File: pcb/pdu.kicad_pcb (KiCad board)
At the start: 2 copper layers, 210 x 105.5 mm, 22 parts, among them J1 XT90-F, J10 XT60-F, J12 Conn_02x06_Odd_Even, J2 XT90-M, J3 XT90-M, J4 XT90-F, J5 XT60-F, J6 XT60-F, J7 XT60-F, J8 XT60-F, J9 XT60-F

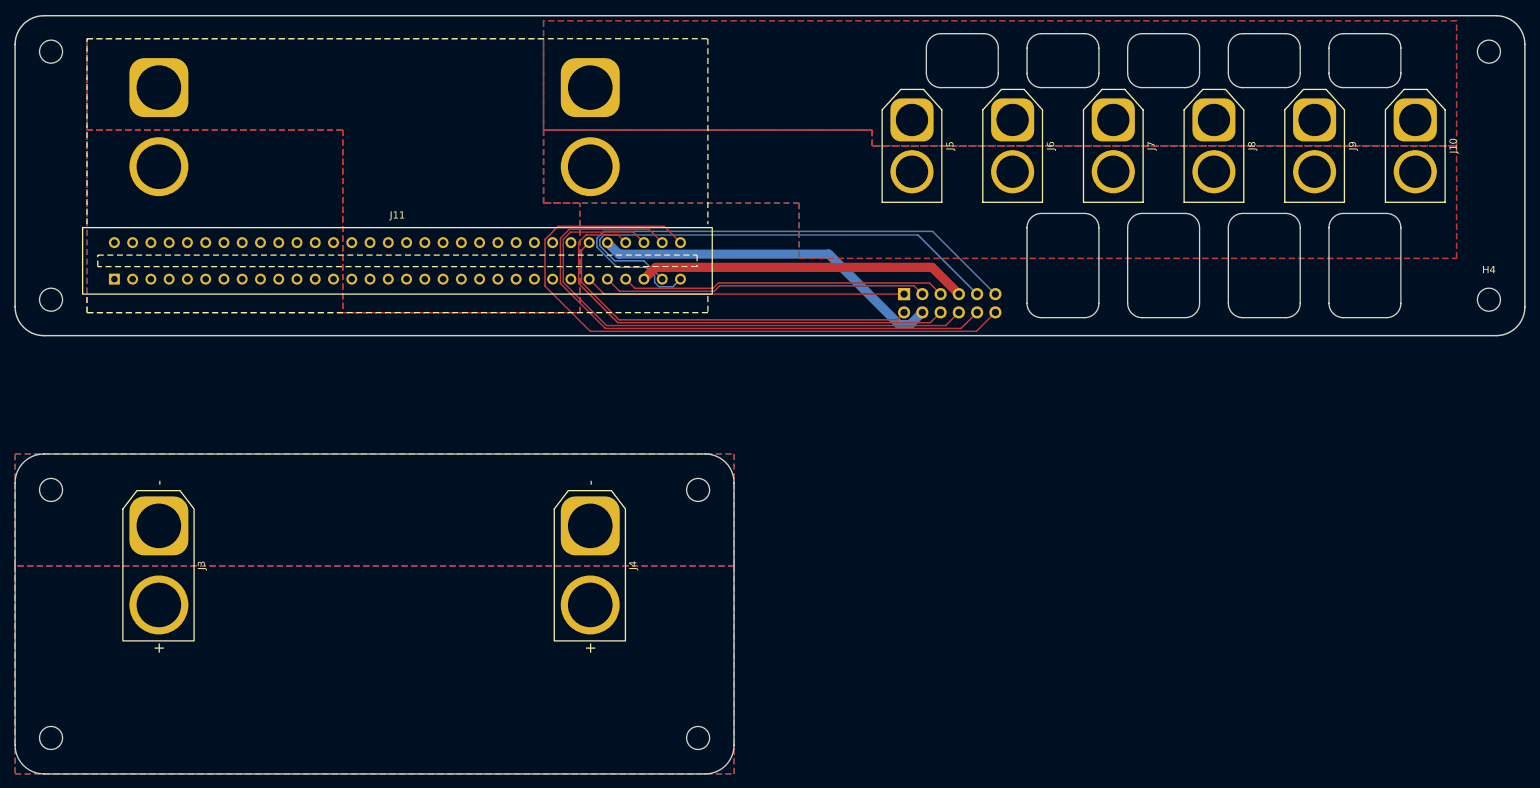
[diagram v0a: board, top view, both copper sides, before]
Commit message: feat: ERC and DRC in CI
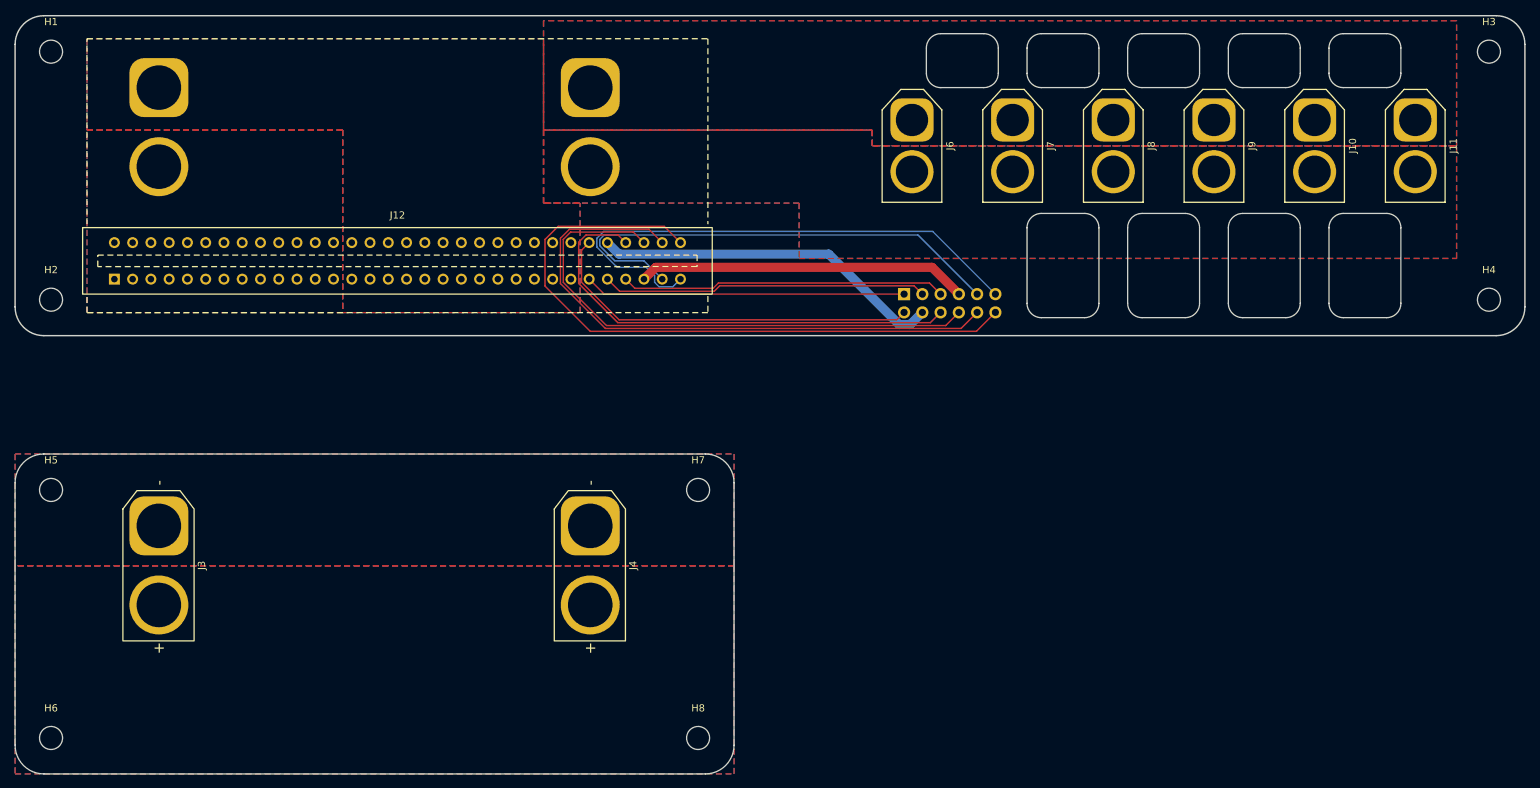
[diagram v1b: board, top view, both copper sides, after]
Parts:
- B1, B2: footprint PCM_kikit:Board -> kikit:Board
- renumbered J9 to J10, J10 to J11, J11 to J12, J12 to J5, J5 to J6, J6 to J7, J7 to J8, J8 to J9
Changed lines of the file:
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@@
 		(descr "AMASS female XT60, through hole, vertical, https://www.tme.eu/Document/2d152ced3b7a446066e6c419d84bb460/XT60%20SPEC.pdf")
 		(tags "XT60 female vertical")
-		(property "Reference" "J6"
+		(property "Reference" "J7"
 			(at 3.6 -5.3 90)
 			(layer "F.SilkS")
@@
 			(at 0 -4.15 0)
 			(layer "F.SilkS")
-			(hide yes)
 			(effects
 				(font
@@
 		(embedded_fonts no)
 	)
-	(footprint "PCM_kikit:Board"
+	(footprint "kikit:Board"
 		(layer "F.Cu")
 		(at 48.5 143.71)
 		(descr "Mark board for extraction")
 		(property "Reference" "B2"
-			(at 0 -5 0)
+			(at -4.5 -5 0)
 			(layer "Dwgs.User")
 			(effects
@@
 		(sheetname "/")
 		(sheetfile "pdu.kicad_sch")
+		(attr through_hole)
 		(fp_poly
 			(pts
@@
 			(at 0 -4.15 0)
 			(layer "F.SilkS")
-			(hide yes)
 			(effects
 				(font
@@
 		(descr "AMASS female XT60, through hole, vertical, https://www.tme.eu/Document/2d152ced3b7a446066e6c419d84bb460/XT60%20SPEC.pdf")
 		(tags "XT60 female vertical")
-		(property "Reference" "J7"
+		(property "Reference" "J8"
 			(at 3.6 -5.3 90)
 			(layer "F.SilkS")
@@
 		(descr "AMASS female XT60, through hole, vertical, https://www.tme.eu/Document/2d152ced3b7a446066e6c419d84bb460/XT60%20SPEC.pdf")
 		(tags "XT60 female vertical")
-		(property "Reference" "J10"
+		(property "Reference" "J11"
 			(at 3.6 -5.3 90)
 			(layer "F.SilkS")
@@
 			(at 0 -4.15 0)
 			(layer "F.SilkS")
-			(hide yes)
 			(effects
 				(font
@@
 		(embedded_fonts no)
 	)
-	(footprint "PCM_kikit:Board"
+	(footprint "kikit:Board"
 		(layer "F.Cu")
 		(at 48.5 82.75)
 		(descr "Mark board for extraction")
 		(property "Reference" "B1"
-			(at 0 -5 0)
+			(at -4.5 -5 0)
 			(layer "Dwgs.User")
 			(effects
@@
 			(at 0 -4.15 0)
 			(layer "F.SilkS")
-			(hide yes)
 			(effects
 				(font
@@
 		(descr "AMASS female XT60, through hole, vertical, https://www.tme.eu/Document/2d152ced3b7a446066e6c419d84bb460/XT60%20SPEC.pdf")
 		(tags "XT60 female vertical")
-		(property "Reference" "J8"
+		(property "Reference" "J9"
 			(at 3.6 -5.3 90)
 			(layer "F.SilkS")
@@
 		(descr "AMASS female XT60, through hole, vertical, https://www.tme.eu/Document/2d152ced3b7a446066e6c419d84bb460/XT60%20SPEC.pdf")
 		(tags "XT60 female vertical")
-		(property "Reference" "J5"
+		(property "Reference" "J6"
 			(at 3.6 -5.3 90)
 			(layer "F.SilkS")
@@
 		(sheetname "/")
 		(sheetfile "pdu.kicad_sch")
+		(attr through_hole)
 		(fp_poly
 			(pts
@@
 			(at 0 -4.15 0)
 			(layer "F.SilkS")
-			(hide yes)
 			(effects
 				(font
@@
 		(descr "AMASS female XT60, through hole, vertical, https://www.tme.eu/Document/2d152ced3b7a446066e6c419d84bb460/XT60%20SPEC.pdf")
 		(tags "XT60 female vertical")
-		(property "Reference" "J9"
+		(property "Reference" "J10"
 			(at 3.6 -5.3 90)
 			(layer "F.SilkS")
@@
 			(at 0 -4.15 0)
 			(layer "F.SilkS")
-			(hide yes)
 			(effects
 				(font
@@
 		(layer "F.Cu")
 		(at 96.68 116.85)
-		(property "Reference" "J11"
+		(property "Reference" "J12"
 			(at 0 -6.35 0)
 			(layer "F.SilkS")
@@
 			)
 		)
-		(property "Datasheet" ""
+		(property "Datasheet" "https://github.com/KCORES/KCORES-CSPS-to-ATX-Converter/blob/main/Document/Datasheet/WingTAT%20S-xxM-2.54-x-xx.pdf"
 			(at 0 0 0)
 			(layer "F.Fab")
@@
 			)
 		)
-		(property "JLC_3DModel_Q" "846b4b9a13594151a20d7c0686635ee3"
-			(at 0 0 0)
-			(layer "Cmts.User")
-			(hide yes)
-			(effects
-				(font
-					(size 1.27 1.27)
-					(thickness 0.15)
-				)
-			)
-		)
-		(property "JLC_3D_Size" "87.57 20.68"
-			(at 0 0 0)
-			(layer "Cmts.User")
-			(hide yes)
-			(effects
-				(font
-					(size 1.27 1.27)
-					(thickness 0.15)
-				)
-			)
-		)
-		(property "Manufacturer Part" "S-64L-2.54-5"
-			(at 0 0 0)
-			(unlocked yes)
-			(layer "F.Fab")
-			(hide yes)
-			(effects
-				(font
-					(size 1 1)
-					(thickness 0.15)
-				)
-			)
-		)
-		(property "Supplier Part" "C9900001011"
-			(at 0 0 0)
-			(unlocked yes)
-			(layer "F.Fab")
-			(hide yes)
-			(effects
-				(font
-					(size 1 1)
-					(thickness 0.15)
-				)
-			)
-		)
-		(property "Supplier" "LCSC"
-			(at 0 0 0)
-			(unlocked yes)
-			(layer "F.Fab")
-			(hide yes)
-			(effects
-				(font
-					(size 1 1)
-					(thickness 0.15)
-				)
-			)
-		)
-		(property "LCSC Part Name" "S-64L-2.54-5"
-			(at 0 0 0)
-			(unlocked yes)
-			(layer "F.Fab")
-			(hide yes)
-			(effects
-				(font
-					(size 1 1)
-					(thickness 0.15)
-				)
-			)
-		)
 		(sheetname "/backplane/psu/")
 		(sheetfile "psu.kicad_sch")
+		(attr through_hole)
 		(fp_rect
 			(start -43.7875 -4.625)
@@
 		)
 		(embedded_fonts no)
-		(model "${KIPRJMOD}/EASYEDA_MODELS/CONN-TH_64P-P2.54_S-64L-2.54-5.step"
-			(offset
-				(xyz 0 -7.55 -5)
-			)
-			(scale
-				(xyz 1 1 1)
-			)
-			(rotate
-				(xyz -0 -0 -0)
-			)
-		)
 	)
 	(footprint "MountingHole:MountingHole_3.2mm_M3"
@@
 			(at 0 -4.15 0)
 			(layer "F.SilkS")
-			(hide yes)
 			(effects
 				(font
@@
 		(sheetname "/")
 		(sheetfile "pdu.kicad_sch")
+		(attr through_hole)
 		(fp_poly
 			(pts
@@
 		(descr "Through hole straight pin header, 2x06, 2.54mm pitch, double rows")
 		(tags "Through hole pin header THT 2x06 2.54mm double row")
-		(property "Reference" "J12"
+		(property "Reference" "J5"
 			(at 1.27 2.38 90)
 			(layer "B.SilkS")
@@
 			(layer "B.SilkS")
 		)
-		(fp_line
+		(fp_rect
 			(start -1.77 1.77)
-			(end -1.77 -14.47)
-			(stroke
-				(width 0.05)
-				(type solid)
-			)
-			(layer "B.CrtYd")
-		)
-		(fp_line
-			(start 4.32 1.77)
-			(end -1.77 1.77)
-			(stroke
-				(width 0.05)
-				(type solid)
-			)
-			(layer "B.CrtYd")
-		)
-		(fp_line
-			(start -1.77 -14.47)
 			(end 4.32 -14.47)
 			(stroke
@@
 				(type solid)
 			)
-			(layer "B.CrtYd")
-		)
-		(fp_line
-			(start 4.32 -14.47)
-			(end 4.32 1.77)
-			(stroke
-				(width 0.05)
-				(type solid)
-			)
+			(fill no)
 			(layer "B.CrtYd")
 		)
@@
 		)
 		(fp_text user "${REFERENCE}"
-			(at 1.27 -6.35 0)
+			(at 1.27 -6.35 180)
 			(layer "B.Fab")
 			(effects
@@
 		(sheetname "/")
 		(sheetfile "pdu.kicad_sch")
+		(attr through_hole)
 		(fp_poly
 			(pts
